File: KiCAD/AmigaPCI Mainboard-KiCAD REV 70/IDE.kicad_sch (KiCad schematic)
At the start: 37 parts, among them CN900 PRIMARY IDE, CN901 SECONDARY IDE, Q900 MMBT3906, U220 74LVC08, U815 74LVC08, U900 74LVC245, U901 74LVC245, U902 74LVC245, U903 74LVC245, U904 74LVC245, U905 74LVC245, U906 74LVC373, U907 74LVC373

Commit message: Add JLCPCB part numbers and fix 74LVC244 footprints.
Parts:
- C900, C901, C902, C904, C905, C906, C907, C908: LCSC (none) -> C14663
- CN900, CN901: LCSC (none) -> C429965
- Q900: LCSC (none) -> C75549
- R215: LCSC (none) -> C23345
- R900: LCSC (none) -> C21190
- R901, R902, R903, R904, R911, R912: LCSC (none) -> C25804
- R906: LCSC (none) -> C22962
- RN900, RN901, RN902, RN903, RN904, RN905, RN906: LCSC (none) -> C12008
- U220, U815: LCSC (none) -> C6053
- U900, U901, U902, U903, U904, U905: LCSC (none) -> C7848
- U906, U907: LCSC (none) -> C485083

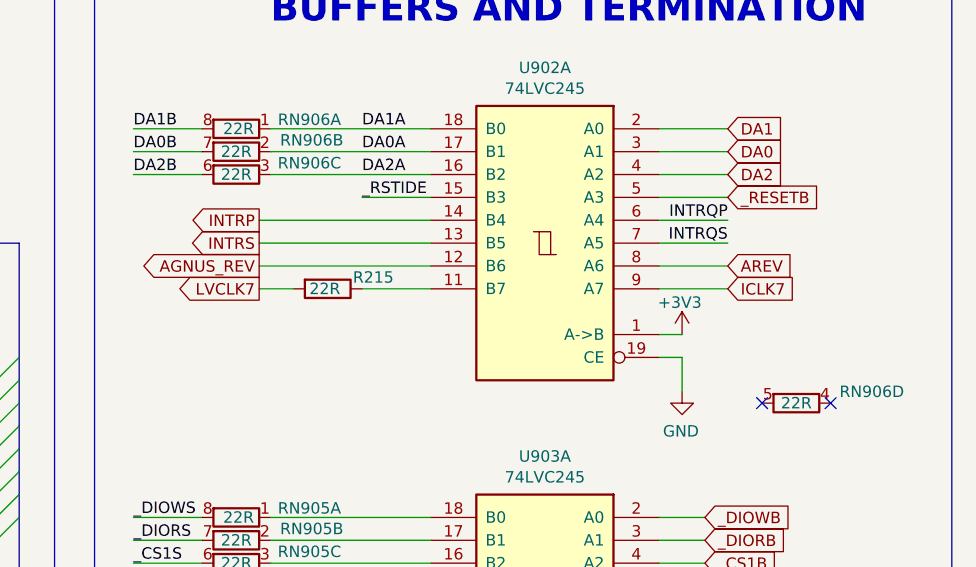
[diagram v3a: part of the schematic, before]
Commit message: Updates to revision 7 board.
Change U810 to 74LVC245 buffers
Add CDAC to U712
Add address latch to CIAs
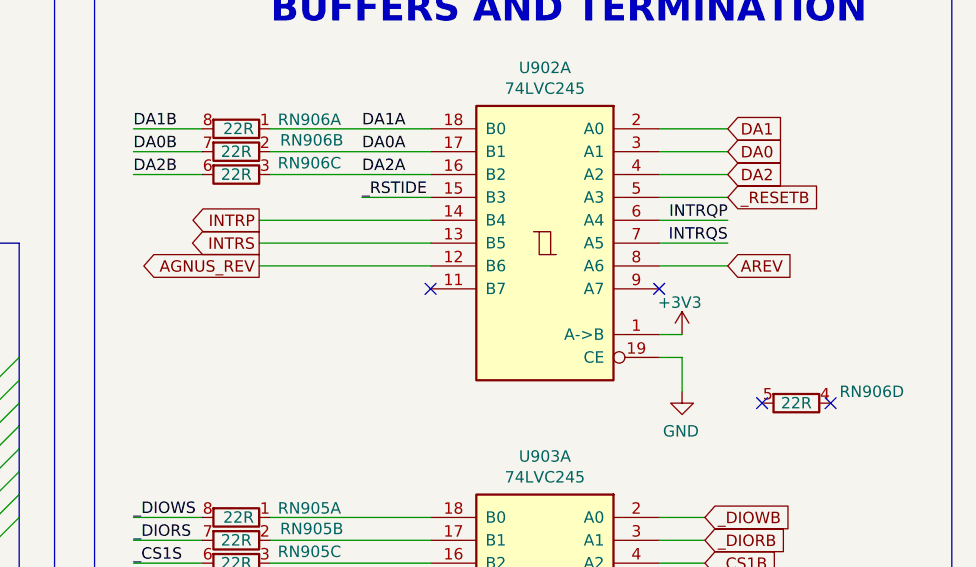
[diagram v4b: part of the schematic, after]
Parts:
- removed R215: 22R, Resistor_SMD:R_0603_1608Metric, symbol Device:R
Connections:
- net ICLK7: no longer names the net of U902.9 (A7)
- no-connect marks 10 -> 12
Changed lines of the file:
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@@
 	(title_block
 		(title "AMIGA PCI")
-		(date "2026-04-27")
+		(date "2026-06-06")
 		(rev "7.0")
 	)
@@
 	)
 	(no_connect
+		(at 240.03 57.15)
+	)
+	(no_connect
 		(at 198.12 219.71)
 	)
@@
 		(at 96.52 214.63)
 	)
+	(no_connect
+		(at 265.43 57.15)
+	)
 	(bus_entry
 		(at 194.31 121.92)
@@
 		)
 	)
-	(wire
-		(pts
-			(xy 220.98 57.15) (xy 224.79 57.15)
-		)
-		(stroke
-			(width 0)
-			(type default)
-		)
-	)
 	(bus
 		(pts
@@
 	(wire
 		(pts
-			(xy 265.43 57.15) (xy 273.05 57.15)
-		)
-		(stroke
-			(width 0)
-			(type default)
-		)
-	)
-	(wire
-		(pts
 			(xy 39.37 92.71) (xy 46.99 92.71)
 		)
@@
 	(wire
 		(pts
-			(xy 232.41 57.15) (xy 240.03 57.15)
-		)
-		(stroke
-			(width 0)
-			(type default)
-		)
-	)
-	(wire
-		(pts
 			(xy 349.25 190.5) (xy 359.41 190.5)
 		)
@@
 		)
 	)
-	(global_label "LVCLK7"
-		(shape output)
-		(at 220.98 57.15 180)
-		(fields_autoplaced yes)
-		(effects
-			(font
-				(size 1.27 1.27)
-			)
-			(justify right)
-		)
-		(property "Intersheetrefs" "${INTERSHEET_REFS}"
-			(at 211.1005 57.15 0)
-			(effects
-				(font
-					(size 1.27 1.27)
-				)
-				(justify right)
-			)
-		)
-	)
 	(global_label "_DIOWB"
 		(shape input)
@@
 		)
 	)
-	(global_label "ICLK7"
-		(shape input)
-		(at 273.05 57.15 0)
-		(fields_autoplaced yes)
-		(effects
-			(font
-				(size 1.27 1.27)
-			)
-			(justify left)
-		)
-		(property "Intersheetrefs" "${INTERSHEET_REFS}"
-			(at 281.4176 57.15 0)
-			(effects
-				(font
-					(size 1.27 1.27)
-				)
-				(justify left)
-			)
-		)
-	)
 	(global_label "DA0"
 		(shape input)
@@
 				)
 			)
-		)
-	)
-	(symbol
-		(lib_id "Device:R")
-		(at 228.6 57.15 270)
-		(unit 1)
-		(exclude_from_sim no)
-		(in_bom yes)
-		(on_board yes)
-		(dnp no)
-		(property "Reference" "R215"
-			(at 231.394 55.88 90)
-			(effects
-				(font
-					(size 1.27 1.27)
-				)
-				(justify left)
-			)
-		)
-		(property "Value" "22R"
-			(at 226.568 57.15 90)
-			(effects
-				(font
-					(size 1.27 1.27)
-				)
-				(justify left)
-			)
-		)
-		(property "Footprint" "Resistor_SMD:R_0603_1608Metric"
-			(at 228.6 55.372 90)
-			(effects
-				(font
-					(size 1.27 1.27)
-				)
-				(hide yes)
-			)
-		)
-		(property "Datasheet" "~"
-			(at 228.6 57.15 0)
-			(effects
-				(font
-					(size 1.27 1.27)
-				)
-				(hide yes)
-			)
-		)
-		(property "Description" ""
-			(at 228.6 57.15 0)
-			(effects
-				(font
-					(size 1.27 1.27)
-				)
-				(hide yes)
-			)
-		)
-		(property "LCSC" "C23345"
-			(at 228.6 57.15 0)
-			(effects
-				(font
-					(size 1.27 1.27)
-				)
-				(hide yes)
-			)
-		)
-		(pin "1"
-		)
-		(pin "2"
-		)
-		(instances
-			(project "AmigaPCI Mainboard"
-				(path "/72453515-27fe-4336-91f3-e3c8054f7767/7a35a97e-5686-44dd-976e-0306b0eb5ef2"
-					(reference "R215")
-					(unit 1)
-				)
-			)
